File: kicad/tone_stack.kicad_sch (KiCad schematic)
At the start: 4 parts

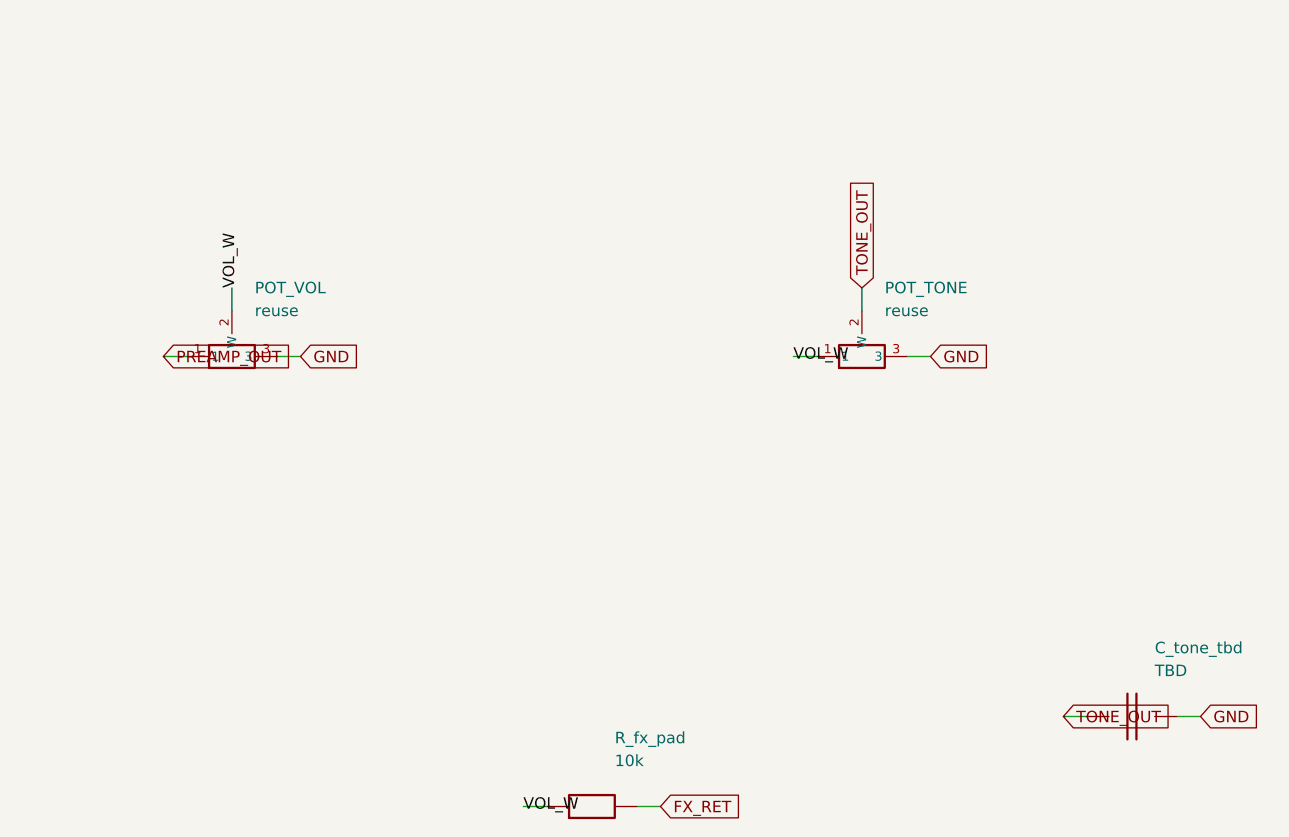
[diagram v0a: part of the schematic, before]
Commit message: Schematic passes KiCad 8 ERC (0 violations); add op-amp mid-rail bias
Installed KiCad 8.0.9 and ran a real Electrical Rules Check on the generated
hierarchy. Drove it to 0 violations:
- snapped every pin/wire endpoint to the 1.27 mm connection grid (was 338
  endpoint_off_grid violations)
- gave the footswitch lines FS_REV/FS_TREM/FS_MRB a real second endpoint via
  100k control pulldowns on the reverb/tremolo/mrb sheets (was 3 dangling labels)

Also made the single-supply TL072 stages electrically real: added a mid-rail
VBIAS network (R_vb1/R_vb2 + C_vb on the Power Supply sheet) and referenced the
reverb driver and tremolo LFO inputs/gain-returns to VBIAS instead of GND
(design addition, flagged in the sheet notes).

Result: kicad-cli 8.0.9 sch erc -> 0 violations; netlist 102 components, 58
nets, 0 unconnected pins; VBIAS spans 10 nodes. Updated SCHEMATIC-BUILD.md,
kicad/README.md, CHANGELOG.md.

https://claude.ai/code/session_01PkrfUi9tvZfLvudJ7h23qD
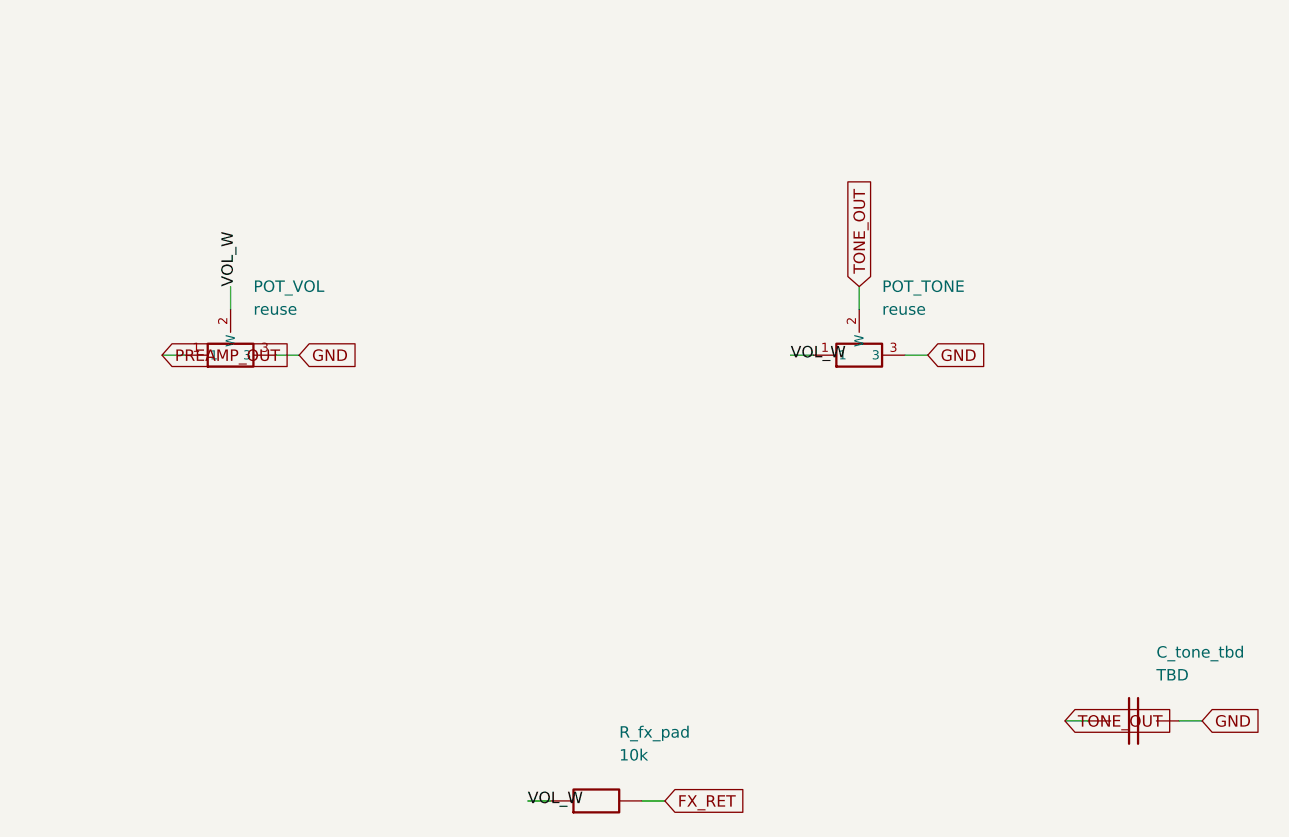
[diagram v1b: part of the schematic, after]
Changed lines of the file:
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@@
   (title_block (title "Vox Cambridge Reverb -- Tone Stack") (company "Reconstructed"))
   (text "TONE STACK -- Vox top-boost network. VALUES TBD (cross-check #4): replicate 25-5274-2." (at 40 20 0) (effects (font (size 1.5 1.5)) (justify left)))
-  (symbol (lib_id "cr_primitives:POT") (at 70 70 0) (unit 1)
+  (symbol (lib_id "cr_primitives:POT") (at 69.85 69.85 0) (unit 1)
     (in_bom yes) (on_board yes) (dnp no)
-    (property "Reference" "POT_VOL" (at 72.54 62.38 0) (effects (font (size 1.27 1.27)) (justify left)))
-    (property "Value" "reuse" (at 72.54 64.92 0) (effects (font (size 1.27 1.27)) (justify left)))
-    (property "Footprint" "" (at 70 70 0) (effects (font (size 1.27 1.27)) hide))
+    (property "Reference" "POT_VOL" (at 72.39 62.23 0) (effects (font (size 1.27 1.27)) (justify left)))
+    (property "Value" "reuse" (at 72.39 64.77 0) (effects (font (size 1.27 1.27)) (justify left)))
+    (property "Footprint" "" (at 69.85 69.85 0) (effects (font (size 1.27 1.27)) hide))
     (pin "1")
     (pin "3")
     (pin "2")
-    (instances (project "cambridge_reverb" (path "/b72d593c-2b6d-4e9f-b9e3-997608c51d97" (reference "POT_VOL") (unit 1))))
+    (instances (project "cambridge_reverb" (path "/810330d3-ecc5-4f4b-8362-4c7e23be2bef" (reference "POT_VOL") (unit 1))))
   )
-  (wire (pts (xy 64.92 70) (xy 62.38 70.0)) (stroke (width 0) (type default)))
-  (global_label "PREAMP_OUT" (shape input) (at 62.38 70.0 180) (fields_autoplaced) (effects (font (size 1.27 1.27)) (justify left)))
-  (wire (pts (xy 75.08 70) (xy 77.62 70.0)) (stroke (width 0) (type default)))
-  (global_label "GND" (shape input) (at 77.62 70.0 0) (fields_autoplaced) (effects (font (size 1.27 1.27)) (justify left)))
-  (wire (pts (xy 70 64.92) (xy 70.0 62.38)) (stroke (width 0) (type default)))
-  (label "VOL_W" (at 70.0 62.38 90) (effects (font (size 1.27 1.27)) (justify left)))
-  (symbol (lib_id "cr_primitives:POT") (at 140 70 0) (unit 1)
+  (wire (pts (xy 64.77 69.85) (xy 62.23 69.85)) (stroke (width 0) (type default)))
+  (global_label "PREAMP_OUT" (shape input) (at 62.23 69.85 180) (fields_autoplaced) (effects (font (size 1.27 1.27)) (justify left)))
+  (wire (pts (xy 74.92999999999999 69.85) (xy 77.47 69.85)) (stroke (width 0) (type default)))
+  (global_label "GND" (shape input) (at 77.47 69.85 0) (fields_autoplaced) (effects (font (size 1.27 1.27)) (justify left)))
+  (wire (pts (xy 69.85 64.77) (xy 69.85 62.23)) (stroke (width 0) (type default)))
+  (label "VOL_W" (at 69.85 62.23 90) (effects (font (size 1.27 1.27)) (justify left)))
+  (symbol (lib_id "cr_primitives:POT") (at 139.7 69.85 0) (unit 1)
     (in_bom yes) (on_board yes) (dnp no)
-    (property "Reference" "POT_TONE" (at 142.54 62.38 0) (effects (font (size 1.27 1.27)) (justify left)))
-    (property "Value" "reuse" (at 142.54 64.92 0) (effects (font (size 1.27 1.27)) (justify left)))
-    (property "Footprint" "" (at 140 70 0) (effects (font (size 1.27 1.27)) hide))
+    (property "Reference" "POT_TONE" (at 142.23999999999998 62.23 0) (effects (font (size 1.27 1.27)) (justify left)))
+    (property "Value" "reuse" (at 142.23999999999998 64.77 0) (effects (font (size 1.27 1.27)) (justify left)))
+    (property "Footprint" "" (at 139.7 69.85 0) (effects (font (size 1.27 1.27)) hide))
     (pin "1")
     (pin "3")
     (pin "2")
-    (instances (project "cambridge_reverb" (path "/b72d593c-2b6d-4e9f-b9e3-997608c51d97" (reference "POT_TONE") (unit 1))))
+    (instances (project "cambridge_reverb" (path "/810330d3-ecc5-4f4b-8362-4c7e23be2bef" (reference "POT_TONE") (unit 1))))
   )
-  (wire (pts (xy 134.92 70) (xy 132.38 70.0)) (stroke (width 0) (type default)))
-  (label "VOL_W" (at 132.38 70.0 180) (effects (font (size 1.27 1.27)) (justify left)))
-  (wire (pts (xy 145.08 70) (xy 147.62 70.0)) (stroke (width 0) (type default)))
-  (global_label "GND" (shape input) (at 147.62 70.0 0) (fields_autoplaced) (effects (font (size 1.27 1.27)) (justify left)))
-  (wire (pts (xy 140 64.92) (xy 140.0 62.38)) (stroke (width 0) (type default)))
-  (global_label "TONE_OUT" (shape input) (at 140.0 62.38 90) (fields_autoplaced) (effects (font (size 1.27 1.27)) (justify left)))
-  (symbol (lib_id "cr_primitives:R") (at 110 120 0) (unit 1)
+  (wire (pts (xy 134.61999999999998 69.85) (xy 132.07999999999998 69.85)) (stroke (width 0) (type default)))
+  (label "VOL_W" (at 132.07999999999998 69.85 180) (effects (font (size 1.27 1.27)) (justify left)))
+  (wire (pts (xy 144.78 69.85) (xy 147.32 69.85)) (stroke (width 0) (type default)))
+  (global_label "GND" (shape input) (at 147.32 69.85 0) (fields_autoplaced) (effects (font (size 1.27 1.27)) (justify left)))
+  (wire (pts (xy 139.7 64.77) (xy 139.7 62.23)) (stroke (width 0) (type default)))
+  (global_label "TONE_OUT" (shape input) (at 139.7 62.23 90) (fields_autoplaced) (effects (font (size 1.27 1.27)) (justify left)))
+  (symbol (lib_id "cr_primitives:R") (at 110.49 119.38 0) (unit 1)
     (in_bom yes) (on_board yes) (dnp no)
-    (property "Reference" "R_fx_pad" (at 112.54 112.38 0) (effects (font (size 1.27 1.27)) (justify left)))
-    (property "Value" "10k" (at 112.54 114.92 0) (effects (font (size 1.27 1.27)) (justify left)))
-    (property "Footprint" "" (at 110 120 0) (effects (font (size 1.27 1.27)) hide))
+    (property "Reference" "R_fx_pad" (at 113.03 111.75999999999999 0) (effects (font (size 1.27 1.27)) (justify left)))
+    (property "Value" "10k" (at 113.03 114.3 0) (effects (font (size 1.27 1.27)) (justify left)))
+    (property "Footprint" "" (at 110.49 119.38 0) (effects (font (size 1.27 1.27)) hide))
     (pin "1")
     (pin "2")
-    (instances (project "cambridge_reverb" (path "/b72d593c-2b6d-4e9f-b9e3-997608c51d97" (reference "R_fx_pad") (unit 1))))
+    (instances (project "cambridge_reverb" (path "/810330d3-ecc5-4f4b-8362-4c7e23be2bef" (reference "R_fx_pad") (unit 1))))
   )
-  (wire (pts (xy 104.92 120) (xy 102.38 120.0)) (stroke (width 0) (type default)))
-  (label "VOL_W" (at 102.38 120.0 180) (effects (font (size 1.27 1.27)) (justify left)))
-  (wire (pts (xy 115.08 120) (xy 117.62 120.0)) (stroke (width 0) (type default)))
-  (global_label "FX_RET" (shape input) (at 117.62 120.0 0) (fields_autoplaced) (effects (font (size 1.27 1.27)) (justify left)))
-  (symbol (lib_id "cr_primitives:C") (at 170 110 0) (unit 1)
+  (wire (pts (xy 105.41 119.38) (xy 102.86999999999999 119.38)) (stroke (width 0) (type default)))
+  (label "VOL_W" (at 102.86999999999999 119.38 180) (effects (font (size 1.27 1.27)) (justify left)))
+  (wire (pts (xy 115.57 119.38) (xy 118.11 119.38)) (stroke (width 0) (type default)))
+  (global_label "FX_RET" (shape input) (at 118.11 119.38 0) (fields_autoplaced) (effects (font (size 1.27 1.27)) (justify left)))
+  (symbol (lib_id "cr_primitives:C") (at 170.18 110.49 0) (unit 1)
     (in_bom yes) (on_board yes) (dnp no)
-    (property "Reference" "C_tone_tbd" (at 172.54 102.38 0) (effects (font (size 1.27 1.27)) (justify left)))
-    (property "Value" "TBD" (at 172.54 104.92 0) (effects (font (size 1.27 1.27)) (justify left)))
-    (property "Footprint" "" (at 170 110 0) (effects (font (size 1.27 1.27)) hide))
+    (property "Reference" "C_tone_tbd" (at 172.72 102.86999999999999 0) (effects (font (size 1.27 1.27)) (justify left)))
+    (property "Value" "TBD" (at 172.72 105.41 0) (effects (font (size 1.27 1.27)) (justify left)))
+    (property "Footprint" "" (at 170.18 110.49 0) (effects (font (size 1.27 1.27)) hide))
     (pin "1")
     (pin "2")
-    (instances (project "cambridge_reverb" (path "/b72d593c-2b6d-4e9f-b9e3-997608c51d97" (reference "C_tone_tbd") (unit 1))))
+    (instances (project "cambridge_reverb" (path "/810330d3-ecc5-4f4b-8362-4c7e23be2bef" (reference "C_tone_tbd") (unit 1))))
   )
-  (wire (pts (xy 164.92 110) (xy 162.38 110.0)) (stroke (width 0) (type default)))
-  (global_label "TONE_OUT" (shape input) (at 162.38 110.0 180) (fields_autoplaced) (effects (font (size 1.27 1.27)) (justify left)))
-  (wire (pts (xy 175.08 110) (xy 177.62 110.0)) (stroke (width 0) (type default)))
-  (global_label "GND" (shape input) (at 177.62 110.0 0) (fields_autoplaced) (effects (font (size 1.27 1.27)) (justify left)))
+  (wire (pts (xy 165.1 110.49) (xy 162.56 110.49)) (stroke (width 0) (type default)))
+  (global_label "TONE_OUT" (shape input) (at 162.56 110.49 180) (fields_autoplaced) (effects (font (size 1.27 1.27)) (justify left)))
+  (wire (pts (xy 175.26000000000002 110.49) (xy 177.8 110.49)) (stroke (width 0) (type default)))
+  (global_label "GND" (shape input) (at 177.8 110.49 0) (fields_autoplaced) (effects (font (size 1.27 1.27)) (justify left)))
   (sheet_instances (path "/" (page "1")))
 )

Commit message: Generate auto-placed PCB (102 footprints, GND pour, board outline)
Build cambridge_reverb.kicad_pcb from the schematic via kicad/gen/gen_pcb.py
(KiCad 8 pcbnew API): assign a THT footprint to every component (standard libs
for generics + the project footprints for VTL5C1 and the 1H toroid), place all
102 footprints (off-board connectors on a bottom wiring-edge strip, toroid in a
reserved spot), assign all 58 nets to pads, draw a 190x115 mm Edge.Cuts outline,
and pour a bottom-layer GND plane. Footprint assignments also carry into the
schematic symbols.

The board opens in KiCad and the ratsnest matches the ERC-clean schematic. It is
placed but NOT routed: kicad-cli pcb drc is dominated by 130 unconnected
(unrouted signal nets; GND is poured) plus cosmetic silk/courtyard overlaps from
dense auto-placement at chassis size -- documented in kicad/PCB-NOTES.md with the
remaining hand-work (placement into floor-plan zones, routing, DRC-to-zero,
Gerbers). Net classes (Default/Power/HighCurrent) carry over for routing.

Also: schematic resistor footprint switched to the compact vertical variant;
gitignore DRC/ERC .rpt reports.

https://claude.ai/code/session_01PkrfUi9tvZfLvudJ7h23qD
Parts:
- C_tone_tbd: footprint (none) -> Capacitor_THT:C_Disc_D7.5mm_W2.5mm_P5.00mm
- POT_TONE, POT_VOL: footprint (none) -> Potentiometer_THT:Potentiometer_Alpha_RD901F-40-00D_Single_Vertical
- R_fx_pad: footprint (none) -> Resistor_THT:R_Axial_DIN0207_L6.3mm_D2.5mm_P5.08mm_Vertical
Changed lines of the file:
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@@
     (property "Reference" "POT_VOL" (at 72.39 62.23 0) (effects (font (size 1.27 1.27)) (justify left)))
     (property "Value" "reuse" (at 72.39 64.77 0) (effects (font (size 1.27 1.27)) (justify left)))
-    (property "Footprint" "" (at 69.85 69.85 0) (effects (font (size 1.27 1.27)) hide))
+    (property "Footprint" "Potentiometer_THT:Potentiometer_Alpha_RD901F-40-00D_Single_Vertical" (at 69.85 69.85 0) (effects (font (size 1.27 1.27)) hide))
     (pin "1")
     (pin "3")
     (pin "2")
-    (instances (project "cambridge_reverb" (path "/810330d3-ecc5-4f4b-8362-4c7e23be2bef" (reference "POT_VOL") (unit 1))))
+    (instances (project "cambridge_reverb" (path "/981ed25d-5b6e-45a1-aebc-056e40b91804" (reference "POT_VOL") (unit 1))))
   )
   (wire (pts (xy 64.77 69.85) (xy 62.23 69.85)) (stroke (width 0) (type default)))
@@
     (property "Reference" "POT_TONE" (at 142.23999999999998 62.23 0) (effects (font (size 1.27 1.27)) (justify left)))
     (property "Value" "reuse" (at 142.23999999999998 64.77 0) (effects (font (size 1.27 1.27)) (justify left)))
-    (property "Footprint" "" (at 139.7 69.85 0) (effects (font (size 1.27 1.27)) hide))
+    (property "Footprint" "Potentiometer_THT:Potentiometer_Alpha_RD901F-40-00D_Single_Vertical" (at 139.7 69.85 0) (effects (font (size 1.27 1.27)) hide))
     (pin "1")
     (pin "3")
     (pin "2")
-    (instances (project "cambridge_reverb" (path "/810330d3-ecc5-4f4b-8362-4c7e23be2bef" (reference "POT_TONE") (unit 1))))
+    (instances (project "cambridge_reverb" (path "/981ed25d-5b6e-45a1-aebc-056e40b91804" (reference "POT_TONE") (unit 1))))
   )
   (wire (pts (xy 134.61999999999998 69.85) (xy 132.07999999999998 69.85)) (stroke (width 0) (type default)))
@@
     (property "Reference" "R_fx_pad" (at 113.03 111.75999999999999 0) (effects (font (size 1.27 1.27)) (justify left)))
     (property "Value" "10k" (at 113.03 114.3 0) (effects (font (size 1.27 1.27)) (justify left)))
-    (property "Footprint" "" (at 110.49 119.38 0) (effects (font (size 1.27 1.27)) hide))
+    (property "Footprint" "Resistor_THT:R_Axial_DIN0207_L6.3mm_D2.5mm_P5.08mm_Vertical" (at 110.49 119.38 0) (effects (font (size 1.27 1.27)) hide))
     (pin "1")
     (pin "2")
-    (instances (project "cambridge_reverb" (path "/810330d3-ecc5-4f4b-8362-4c7e23be2bef" (reference "R_fx_pad") (unit 1))))
+    (instances (project "cambridge_reverb" (path "/981ed25d-5b6e-45a1-aebc-056e40b91804" (reference "R_fx_pad") (unit 1))))
   )
   (wire (pts (xy 105.41 119.38) (xy 102.86999999999999 119.38)) (stroke (width 0) (type default)))
@@
     (property "Reference" "C_tone_tbd" (at 172.72 102.86999999999999 0) (effects (font (size 1.27 1.27)) (justify left)))
     (property "Value" "TBD" (at 172.72 105.41 0) (effects (font (size 1.27 1.27)) (justify left)))
-    (property "Footprint" "" (at 170.18 110.49 0) (effects (font (size 1.27 1.27)) hide))
+    (property "Footprint" "Capacitor_THT:C_Disc_D7.5mm_W2.5mm_P5.00mm" (at 170.18 110.49 0) (effects (font (size 1.27 1.27)) hide))
     (pin "1")
     (pin "2")
-    (instances (project "cambridge_reverb" (path "/810330d3-ecc5-4f4b-8362-4c7e23be2bef" (reference "C_tone_tbd") (unit 1))))
+    (instances (project "cambridge_reverb" (path "/981ed25d-5b6e-45a1-aebc-056e40b91804" (reference "C_tone_tbd") (unit 1))))
   )
   (wire (pts (xy 165.1 110.49) (xy 162.56 110.49)) (stroke (width 0) (type default)))
